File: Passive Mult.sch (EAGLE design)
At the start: 10 parts, among them J1 OG-PJ301_PJ301_THONKICONN4, J2 OG-PJ301_PJ301_THONKICONN4, J3 OG-PJ301_PJ301_THONKICONN4, J4 OG-PJ301_PJ301_THONKICONN4, J5 OG-PJ301_PJ301_THONKICONN4, J6 OG-PJ301_PJ301_THONKICONN4, J7 OG-PJ301_PJ301_THONKICONN4, J8 OG-PJ301_PJ301_THONKICONN4

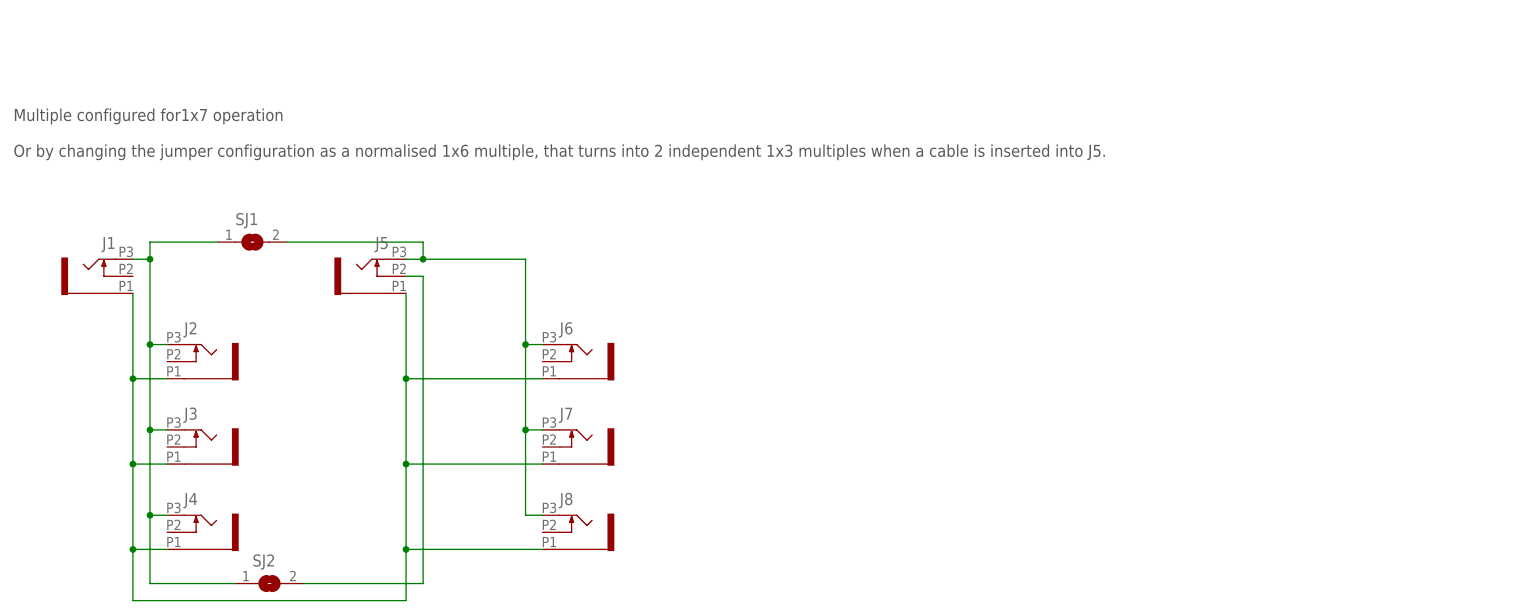
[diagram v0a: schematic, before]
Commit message: BottomSilk updated, front-panel holes and dimension dxf added
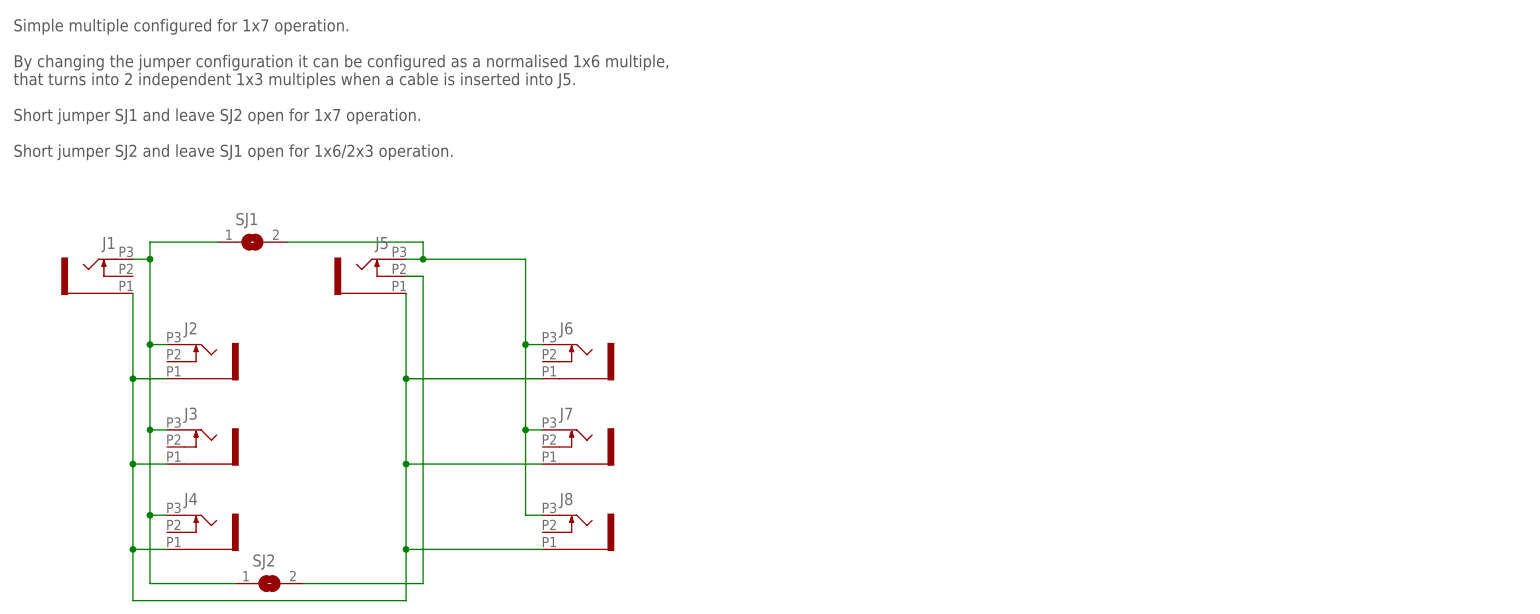
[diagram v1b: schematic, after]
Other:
- note added: "Simple multiple configured for 1x7 operation. By changing the jumper configuration it can be configured as a normalised 1x6 multiple, that turns into 2 independent 1x3 multiples when a cable is inserted into J5. Short jumper SJ1 and leave SJ2 open for 1x7 operation. Short jumper SJ2 and leave SJ1 open for 1x6/2x3 operation."
- note removed: "Multiple configured for1x7 operation Or by changing the jumper configuration as a normalised 1x6 multiple, that turns into 2 independent 1x3 multiples when a cable is inserted into J5."
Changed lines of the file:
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@@
 <?xml version="1.0" encoding="utf-8"?>
 <!DOCTYPE eagle SYSTEM "eagle.dtd">
-<eagle version="7.2.0">
+<eagle version="8.0.0">
 <drawing>
 <settings>
@@
 <grid distance="0.1" unitdist="inch" unit="inch" style="lines" multiple="1" display="no" altdistance="0.01" altunitdist="inch" altunit="inch"/>
 <layers>
-<layer number="1" name="Top" color="4" fill="1" visible="yes" active="no"/>
-<layer number="2" name="Route2" color="1" fill="3" visible="yes" active="no"/>
-<layer number="3" name="Route3" color="4" fill="3" visible="yes" active="no"/>
-<layer number="4" name="Route4" color="1" fill="4" visible="yes" active="no"/>
-<layer number="5" name="Route5" color="4" fill="4" visible="yes" active="no"/>
-<layer number="6" name="Route6" color="1" fill="8" visible="yes" active="no"/>
-<layer number="7" name="Route7" color="4" fill="8" visible="yes" active="no"/>
-<layer number="8" name="Route8" color="1" fill="2" visible="yes" active="no"/>
-<layer number="9" name="Route9" color="4" fill="2" visible="yes" active="no"/>
-<layer number="10" name="Route10" color="1" fill="7" visible="yes" active="no"/>
-<layer number="11" name="Route11" color="4" fill="7" visible="yes" active="no"/>
-<layer number="12" name="Route12" color="1" fill="5" visible="yes" active="no"/>
-<layer number="13" name="Route13" color="4" fill="5" visible="yes" active="no"/>
-<layer number="14" name="Route14" color="1" fill="6" visible="yes" active="no"/>
-<layer number="15" name="Route15" color="4" fill="6" visible="yes" active="no"/>
-<layer number="16" name="Bottom" color="1" fill="1" visible="yes" active="no"/>
-<layer number="17" name="Pads" color="2" fill="1" visible="yes" active="no"/>
-<layer number="18" name="Vias" color="2" fill="1" visible="yes" active="no"/>
-<layer number="19" name="Unrouted" color="6" fill="1" visible="yes" active="no"/>
-<layer number="20" name="Dimension" color="15" fill="1" visible="yes" active="no"/>
-<layer number="21" name="tPlace" color="7" fill="1" visible="yes" active="no"/>
-<layer number="22" name="bPlace" color="7" fill="1" visible="yes" active="no"/>
-<layer number="23" name="tOrigins" color="15" fill="1" visible="yes" active="no"/>
-<layer number="24" name="bOrigins" color="15" fill="1" visible="yes" active="no"/>
-<layer number="25" name="tNames" color="7" fill="1" visible="yes" active="no"/>
-<layer number="26" name="bNames" color="7" fill="1" visible="yes" active="no"/>
-<layer number="27" name="tValues" color="7" fill="1" visible="yes" active="no"/>
-<layer number="28" name="bValues" color="7" fill="1" visible="yes" active="no"/>
+<layer number="1" name="Top" color="4" fill="1" visible="no" active="no"/>
+<layer number="2" name="Route2" color="1" fill="3" visible="no" active="no"/>
+<layer number="3" name="Route3" color="4" fill="3" visible="no" active="no"/>
+<layer number="4" name="Route4" color="1" fill="4" visible="no" active="no"/>
+<layer number="5" name="Route5" color="4" fill="4" visible="no" active="no"/>
+<layer number="6" name="Route6" color="1" fill="8" visible="no" active="no"/>
+<layer number="7" name="Route7" color="4" fill="8" visible="no" active="no"/>
+<layer number="8" name="Route8" color="1" fill="2" visible="no" active="no"/>
+<layer number="9" name="Route9" color="4" fill="2" visible="no" active="no"/>
+<layer number="10" name="Route10" color="1" fill="7" visible="no" active="no"/>
+<layer number="11" name="Route11" color="4" fill="7" visible="no" active="no"/>
+<layer number="12" name="Route12" color="1" fill="5" visible="no" active="no"/>
+<layer number="13" name="Route13" color="4" fill="5" visible="no" active="no"/>
+<layer number="14" name="Route14" color="1" fill="6" visible="no" active="no"/>
+<layer number="15" name="Route15" color="4" fill="6" visible="no" active="no"/>
+<layer number="16" name="Bottom" color="1" fill="1" visible="no" active="no"/>
+<layer number="17" name="Pads" color="2" fill="1" visible="no" active="no"/>
+<layer number="18" name="Vias" color="2" fill="1" visible="no" active="no"/>
+<layer number="19" name="Unrouted" color="6" fill="1" visible="no" active="no"/>
+<layer number="20" name="Dimension" color="15" fill="1" visible="no" active="no"/>
+<layer number="21" name="tPlace" color="7" fill="1" visible="no" active="no"/>
+<layer number="22" name="bPlace" color="7" fill="1" visible="no" active="no"/>
+<layer number="23" name="tOrigins" color="15" fill="1" visible="no" active="no"/>
+<layer number="24" name="bOrigins" color="15" fill="1" visible="no" active="no"/>
+<layer number="25" name="tNames" color="7" fill="1" visible="no" active="no"/>
+<layer number="26" name="bNames" color="7" fill="1" visible="no" active="no"/>
+<layer number="27" name="tValues" color="7" fill="1" visible="no" active="no"/>
+<layer number="28" name="bValues" color="7" fill="1" visible="no" active="no"/>
 <layer number="29" name="tStop" color="7" fill="3" visible="no" active="no"/>
 <layer number="30" name="bStop" color="7" fill="6" visible="no" active="no"/>
@@
 <layer number="35" name="tGlue" color="7" fill="4" visible="no" active="no"/>
 <layer number="36" name="bGlue" color="7" fill="5" visible="no" active="no"/>
-<layer number="37" name="tTest" color="7" fill="1" visible="yes" active="no"/>
-<layer number="38" name="bTest" color="7" fill="1" visible="yes" active="no"/>
+<layer number="37" name="tTest" color="7" fill="1" visible="no" active="no"/>
+<layer number="38" name="bTest" color="7" fill="1" visible="no" active="no"/>
 <layer number="39" name="tKeepout" color="4" fill="11" visible="no" active="no"/>
 <layer number="40" name="bKeepout" color="1" fill="11" visible="no" active="no"/>
@@
 <layer number="44" name="Drills" color="7" fill="1" visible="no" active="no"/>
 <layer number="45" name="Holes" color="7" fill="1" visible="no" active="no"/>
-<layer number="46" name="Milling" color="3" fill="1" visible="yes" active="no"/>
-<layer number="47" name="Measures" color="7" fill="1" visible="yes" active="no"/>
-<layer number="48" name="Document" color="7" fill="1" visible="yes" active="no"/>
-<layer number="49" name="Reference" color="7" fill="1" visible="yes" active="no"/>
-<layer number="50" name="dxf" color="7" fill="1" visible="yes" active="no"/>
-<layer number="51" name="tDocu" color="7" fill="1" visible="yes" active="no"/>
-<layer number="52" name="bDocu" color="7" fill="1" visible="yes" active="no"/>
-<layer number="53" name="tGND_GNDA" color="7" fill="1" visible="yes" active="no"/>
-<layer number="54" name="bGND_GNDA" color="7" fill="1" visible="yes" active="no"/>
-<layer number="56" name="wert" color="7" fill="1" visible="yes" active="no"/>
-<layer number="57" name="tCAD" color="7" fill="1" visible="yes" active="no"/>
+<layer number="46" name="Milling" color="3" fill="1" visible="no" active="no"/>
+<layer number="47" name="Measures" color="7" fill="1" visible="no" active="no"/>
+<layer number="48" name="Document" color="7" fill="1" visible="no" active="no"/>
+<layer number="49" name="Reference" color="7" fill="1" visible="no" active="no"/>
+<layer number="50" name="dxf" color="7" fill="1" visible="no" active="no"/>
+<layer number="51" name="tDocu" color="7" fill="1" visible="no" active="no"/>
+<layer number="52" name="bDocu" color="7" fill="1" visible="no" active="no"/>
+<layer number="53" name="tGND_GNDA" color="7" fill="1" visible="no" active="no"/>
+<layer number="54" name="bGND_GNDA" color="7" fill="1" visible="no" active="no"/>
+<layer number="56" name="wert" color="7" fill="1" visible="no" active="no"/>
+<layer number="57" name="tCAD" color="7" fill="1" visible="no" active="no"/>
 <layer number="90" name="Modules" color="5" fill="1" visible="yes" active="yes"/>
 <layer number="91" name="Nets" color="2" fill="1" visible="yes" active="yes"/>
@@
 <sheet>
 <plain>
-<text x="-12.7" y="101.6" size="1.778" layer="97">Multiple configured for1x7 operation
-Or by changing the jumper configuration as a normalised 1x6 multiple, that turns into 2 independent 1x3 multiples when a cable is inserted into J5. </text>
+<text x="-12.7" y="101.6" size="1.778" layer="97">Simple multiple configured for 1x7 operation.
+By changing the jumper configuration it can be configured as a normalised 1x6 multiple,
+that turns into 2 independent 1x3 multiples when a cable is inserted into J5.
+Short jumper SJ1 and leave SJ2 open for 1x7 operation.
+Short jumper SJ2 and leave SJ1 open for 1x6/2x3 operation.</text>
 </plain>
 <instances>
